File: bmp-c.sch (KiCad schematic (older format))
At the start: 61 parts, among them J1 USB_C_Receptacle_USB2.0, J2 Conn_01x10, J3 Conn_01x04, J4 JTAG-10, Q1 DMG1023DV, Q2 DMG1024UV, SW1 SW_SPST, U1 USBLC6-2P6, U2 SN74LVC2T45YZPR, U3 SN74LVC2T45YZPR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

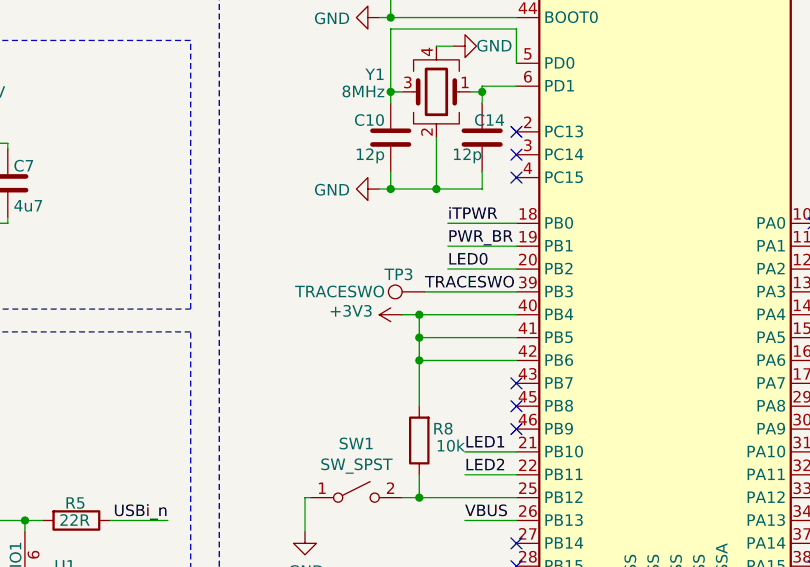
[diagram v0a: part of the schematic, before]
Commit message: remove SWO testpoint
Signed-off-by: Dominik Sliwa <dominik@e-plum.pl>
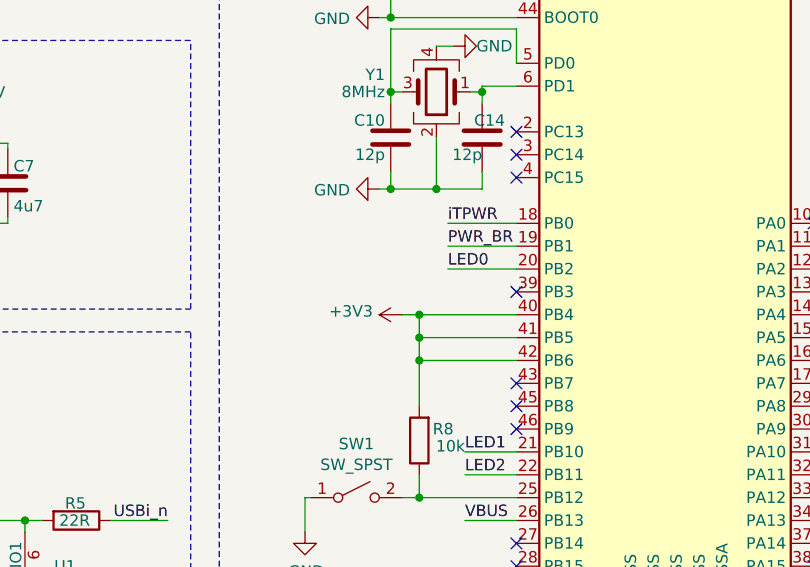
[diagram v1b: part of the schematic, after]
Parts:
- removed TP3: TRACESWO, TestPoint:TestPoint_Pad_D1.0mm, symbol Connector:TestPoint
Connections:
- net TRACESWO: no longer names the net of U6.39 (PB3)
- no-connect marks 13 -> 14
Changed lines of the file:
@@
 Wire Wire Line
 	5450 4375 5150 4375
-Wire Wire Line
-	5450 4475 5050 4475
 Text Label 5150 4275 0    50   ~ 0
 PWR_BR
 Text Label 5150 4375 0    50   ~ 0
 LED0
-Text Label 5050 4475 0    50   ~ 0
-TRACESWO
 Connection ~ 5025 4575
 Wire Wire Line
@@
 Text Label 9350 4825 0    50   ~ 0
 RST
-$Comp
-L Connector:TestPoint TP3
-U 1 1 5E7C2863
-P 5050 4475
-F 0 "TP3" V 5125 4525 50  0000 L CNN
-F 1 "TRACESWO" V 5050 4650 50  0000 L CNN
-F 2 "TestPoint:TestPoint_Pad_D1.0mm" H 5250 4475 50  0001 C CNN
-F 3 "~" H 5250 4475 50  0001 C CNN
-	1    5050 4475
-	0    -1   -1   0
-$EndComp
 Wire Wire Line
 	9575 3150 9350 3150
@@
 Text Label 5825 6225 2    50   ~ 0
 xTPWR
+NoConn ~ 5450 4475
 $EndSCHEMATC

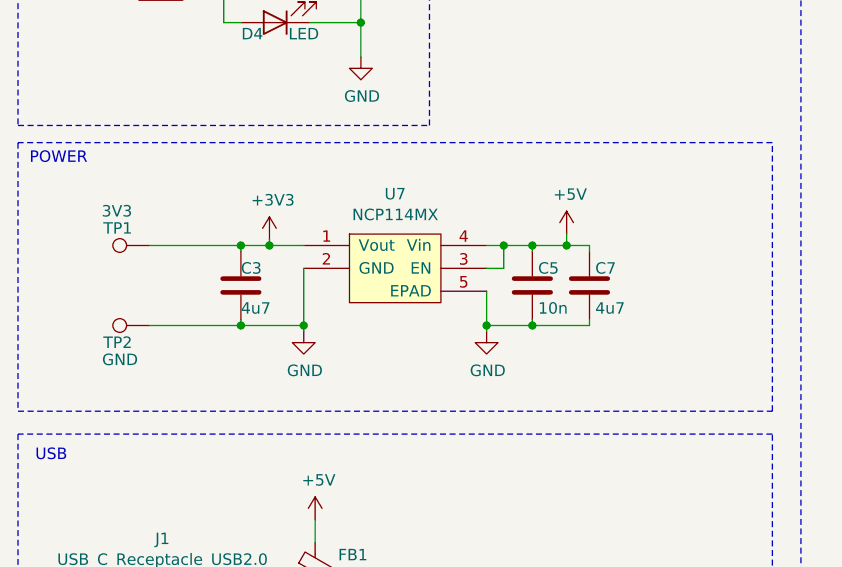
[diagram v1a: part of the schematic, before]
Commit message: use kicad library symbol for ncp114
Signed-off-by: Dominik Sliwa <dominik@e-plum.pl>
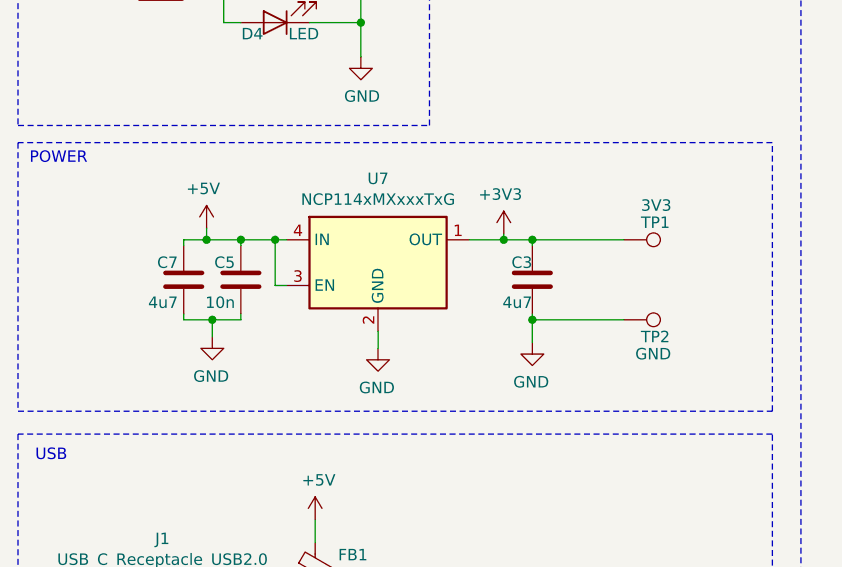
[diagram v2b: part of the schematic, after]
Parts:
- removed U7: NCP114MX, Package_DFN_QFN:UDFN-4_1x1mm_P0.65mm, symbol custom:NCP114MX
- added U7: NCP114xMXxxxTxG, Package_DFN_QFN:UDFN-4_1x1mm_P0.65mm, symbol Regulator_Linear:NCP114xMXxxxTxG
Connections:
- net +3V3: now also U7.1 (OUT)
- net +5V: now also U7.3 (EN), U7.4 (IN)
- net GND: now also U7.2 (GND), U7.5 (GND)
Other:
- moved on the sheet: C3, C5, C7, TP1, TP2
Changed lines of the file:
@@
 L Device:C C5
 U 1 1 5D514B13
-P 2975 4000
-F 0 "C5" H 3000 4075 50  0000 L CNN
-F 1 "10n" H 3000 3900 50  0000 L CNN
-F 2 "Capacitor_SMD:C_0402_1005Metric" H 3013 3850 50  0001 C CNN
-F 3 "~" H 2975 4000 50  0001 C CNN
-	1    2975 4000
-	1    0    0    -1
+P 1700 3975
+F 0 "C5" H 1725 4050 50  0000 L CNN
+F 1 "10n" H 1725 3875 50  0000 L CNN
+F 2 "Capacitor_SMD:C_0402_1005Metric" H 1738 3825 50  0001 C CNN
+F 3 "~" H 1700 3975 50  0001 C CNN
+	1    1700 3975
+	-1   0    0    -1
 $EndComp
 $Comp
 L Device:C C7
 U 1 1 5D515321
-P 3225 4000
-F 0 "C7" H 3250 4075 50  0000 L CNN
-F 1 "4u7" H 3250 3900 50  0000 L CNN
-F 2 "Capacitor_SMD:C_0603_1608Metric" H 3263 3850 50  0001 C CNN
-F 3 "~" H 3225 4000 50  0001 C CNN
-	1    3225 4000
-	1    0    0    -1
+P 1450 3975
+F 0 "C7" H 1475 4050 50  0000 L CNN
+F 1 "4u7" H 1475 3875 50  0000 L CNN
+F 2 "Capacitor_SMD:C_0603_1608Metric" H 1488 3825 50  0001 C CNN
+F 3 "~" H 1450 3975 50  0001 C CNN
+	1    1450 3975
+	-1   0    0    -1
 $EndComp
 $Comp
 L Device:C C3
 U 1 1 5D515C34
-P 1700 4000
-F 0 "C3" H 1700 4075 50  0000 L CNN
-F 1 "4u7" H 1700 3900 50  0000 L CNN
-F 2 "Capacitor_SMD:C_0603_1608Metric" H 1738 3850 50  0001 C CNN
-F 3 "~" H 1700 4000 50  0001 C CNN
-	1    1700 4000
-	1    0    0    -1
-$EndComp
-$Comp
-L custom:NCP114MX U7
-U 1 1 5D51FB0C
-P 2375 3875
-F 0 "U7" H 2375 4150 50  0000 C CNN
-F 1 "NCP114MX" H 2375 4059 50  0000 C CNN
-F 2 "Package_DFN_QFN:UDFN-4_1x1mm_P0.65mm" H 2375 3875 50  0001 C CNN
-F 3 "" H 2375 3875 50  0001 C CNN
-	1    2375 3875
-	1    0    0    -1
+P 2975 3975
+F 0 "C3" H 2975 4050 50  0000 L CNN
+F 1 "4u7" H 2975 3875 50  0000 L CNN
+F 2 "Capacitor_SMD:C_0603_1608Metric" H 3013 3825 50  0001 C CNN
+F 3 "~" H 2975 3975 50  0001 C CNN
+	1    2975 3975
+	-1   0    0    -1
 $EndComp
 $Comp
@@
 L power:GND #PWR09
 U 1 1 5D562287
-P 1975 4200
-F 0 "#PWR09" H 1975 3950 50  0001 C CNN
-F 1 "GND" H 1980 4027 50  0000 C CNN
-F 2 "" H 1975 4200 50  0001 C CNN
-F 3 "" H 1975 4200 50  0001 C CNN
-	1    1975 4200
-	1    0    0    -1
+P 2975 4250
+F 0 "#PWR09" H 2975 4000 50  0001 C CNN
+F 1 "GND" H 2980 4077 50  0000 C CNN
+F 2 "" H 2975 4250 50  0001 C CNN
+F 3 "" H 2975 4250 50  0001 C CNN
+	1    2975 4250
+	-1   0    0    -1
 $EndComp
 $Comp
 L power:GND #PWR016
 U 1 1 5D563C7B
-P 2775 4200
-F 0 "#PWR016" H 2775 3950 50  0001 C CNN
-F 1 "GND" H 2780 4027 50  0000 C CNN
-F 2 "" H 2775 4200 50  0001 C CNN
-F 3 "" H 2775 4200 50  0001 C CNN
-	1    2775 4200
-	1    0    0    -1
-$EndComp
-Wire Wire Line
-	1975 3825 1825 3825
-Wire Wire Line
-	1700 3825 1700 3850
-Wire Wire Line
-	1700 4150 1700 4175
-Wire Wire Line
-	1700 4175 1975 4175
-Wire Wire Line
-	1975 4175 1975 3925
-Wire Wire Line
-	1975 4175 1975 4200
-Connection ~ 1975 4175
-Wire Wire Line
-	2775 3925 2850 3925
-Wire Wire Line
-	2850 3925 2850 3825
-Wire Wire Line
-	2850 3825 2775 3825
-Wire Wire Line
-	2850 3825 2975 3825
-Wire Wire Line
-	3225 3825 3225 3850
-Connection ~ 2850 3825
-Wire Wire Line
-	2975 3850 2975 3825
-Connection ~ 2975 3825
-Wire Wire Line
-	2975 3825 3125 3825
-Wire Wire Line
-	2775 4025 2775 4175
-Wire Wire Line
-	2775 4175 2975 4175
-Wire Wire Line
-	2975 4175 2975 4150
-Connection ~ 2775 4175
-Wire Wire Line
-	2775 4175 2775 4200
-Wire Wire Line
-	3225 4150 3225 4175
-Wire Wire Line
-	3225 4175 2975 4175
-Connection ~ 2975 4175
+P 1575 4225
+F 0 "#PWR016" H 1575 3975 50  0001 C CNN
+F 1 "GND" H 1580 4052 50  0000 C CNN
+F 2 "" H 1575 4225 50  0001 C CNN
+F 3 "" H 1575 4225 50  0001 C CNN
+	1    1575 4225
+	-1   0    0    -1
+$EndComp
+Wire Wire Line
+	2700 3800 2850 3800
+Wire Wire Line
+	2975 3800 2975 3825
+Wire Wire Line
+	2975 4125 2975 4150
+Wire Wire Line
+	1450 3800 1450 3825
+Wire Wire Line
+	1700 3825 1700 3800
+Connection ~ 1700 3800
+Wire Wire Line
+	1700 3800 1550 3800
+Wire Wire Line
+	1700 4150 1700 4125
+Wire Wire Line
+	1450 4125 1450 4150
+Wire Wire Line
+	1450 4150 1575 4150
 $Comp
 L power:+5V #PWR019
 U 1 1 5D57BEAB
-P 3125 3775
-F 0 "#PWR019" H 3125 3625 50  0001 C CNN
-F 1 "+5V" H 3140 3948 50  0000 C CNN
-F 2 "" H 3125 3775 50  0001 C CNN
-F 3 "" H 3125 3775 50  0001 C CNN
-	1    3125 3775
-	1    0    0    -1
-$EndComp
-Wire Wire Line
-	3125 3775 3125 3825
-Connection ~ 3125 3825
-Wire Wire Line
-	3125 3825 3225 3825
+P 1550 3750
+F 0 "#PWR019" H 1550 3600 50  0001 C CNN
+F 1 "+5V" H 1565 3923 50  0000 C CNN
+F 2 "" H 1550 3750 50  0001 C CNN
+F 3 "" H 1550 3750 50  0001 C CNN
+	1    1550 3750
+	-1   0    0    -1
+$EndComp
+Wire Wire Line
+	1550 3750 1550 3800
+Connection ~ 1550 3800
+Wire Wire Line
+	1550 3800 1450 3800
 $Comp
 L power:+3V3 #PWR06
 U 1 1 5D57F918
-P 1825 3800
-F 0 "#PWR06" H 1825 3650 50  0001 C CNN
-F 1 "+3V3" H 1840 3973 50  0000 C CNN
-F 2 "" H 1825 3800 50  0001 C CNN
-F 3 "" H 1825 3800 50  0001 C CNN
-	1    1825 3800
-	1    0    0    -1
-$EndComp
-Wire Wire Line
-	1825 3800 1825 3825
-Connection ~ 1825 3825
-Wire Wire Line
-	1825 3825 1700 3825
+P 2850 3775
+F 0 "#PWR06" H 2850 3625 50  0001 C CNN
+F 1 "+3V3" H 2865 3948 50  0000 C CNN
+F 2 "" H 2850 3775 50  0001 C CNN
+F 3 "" H 2850 3775 50  0001 C CNN
+	1    2850 3775
+	-1   0    0    -1
+$EndComp
+Wire Wire Line
+	2850 3775 2850 3800
+Connection ~ 2850 3800
+Wire Wire Line
+	2850 3800 2975 3800
 Wire Notes Line
 	725  4550 4025 4550
@@
 	1    0    0    -1
 $EndComp
-Connection ~ 1700 3825
-Connection ~ 1700 4175
+Connection ~ 2975 3800
 Wire Wire Line
 	6100 2600 6100 2775
@@
 L Connector:TestPoint TP1
 U 1 1 5D7E637F
-P 1300 3825
-F 0 "TP1" V 1375 3900 50  0000 L CNN
-F 1 "3V3" V 1450 3900 50  0000 L CNN
-F 2 "TestPoint:TestPoint_Pad_D1.0mm" H 1500 3825 50  0001 C CNN
-F 3 "~" H 1500 3825 50  0001 C CNN
-	1    1300 3825
-	0    -1   -1   0
+P 3375 3800
+F 0 "TP1" V 3450 3875 50  0000 L CNN
+F 1 "3V3" V 3525 3875 50  0000 L CNN
+F 2 "TestPoint:TestPoint_Pad_D1.0mm" H 3575 3800 50  0001 C CNN
+F 3 "~" H 3575 3800 50  0001 C CNN
+	1    3375 3800
+	0    1    -1   0
 $EndComp
 $Comp
 L Connector:TestPoint TP2
 U 1 1 5D7E82A3
-P 1300 4175
-F 0 "TP2" V 1225 4250 50  0000 L CNN
-F 1 "GND" V 1150 4225 50  0000 L CNN
-F 2 "TestPoint:TestPoint_Pad_D1.0mm" H 1500 4175 50  0001 C CNN
-F 3 "~" H 1500 4175 50  0001 C CNN
-	1    1300 4175
-	0    -1   -1   0
+P 3375 4150
+F 0 "TP2" V 3300 4225 50  0000 L CNN
+F 1 "GND" V 3225 4200 50  0000 L CNN
+F 2 "TestPoint:TestPoint_Pad_D1.0mm" H 3575 4150 50  0001 C CNN
+F 3 "~" H 3575 4150 50  0001 C CNN
+	1    3375 4150
+	0    1    -1   0
 $EndComp
 NoConn ~ 5450 3775
@@
 	5025 4775 5450 4775
 Wire Wire Line
-	1300 4175 1700 4175
-Wire Wire Line
-	1300 3825 1700 3825
+	3375 4150 2975 4150
+Wire Wire Line
+	3375 3800 2975 3800
 Text Label 5825 6225 2    50   ~ 0
 xTPWR
 NoConn ~ 5450 4475
+$Comp
+L Regulator_Linear:NCP114xMXxxxTxG U7
+U 1 1 5D71C52E
+P 2300 3900
+F 0 "U7" H 2300 4267 50  0000 C CNN
+F 1 "NCP114xMXxxxTxG" H 2300 4176 50  0000 C CNN
+F 2 "Package_DFN_QFN:UDFN-4_1x1mm_P0.65mm" H 3100 3500 50  0001 C CNN
+F 3 "https://www.onsemi.com/pub/Collateral/NCP114-D.PDF" H 2300 3900 50  0001 C CNN
+	1    2300 3900
+	1    0    0    -1
+$EndComp
+$Comp
+L power:GND #PWR048
+U 1 1 5D7FABA9
+P 2300 4275
+F 0 "#PWR048" H 2300 4025 50  0001 C CNN
+F 1 "GND" H 2305 4102 50  0000 C CNN
+F 2 "" H 2300 4275 50  0001 C CNN
+F 3 "" H 2300 4275 50  0001 C CNN
+	1    2300 4275
+	-1   0    0    -1
+$EndComp
+Wire Wire Line
+	1700 3800 1850 3800
+Wire Wire Line
+	2975 4250 2975 4150
+Connection ~ 2975 4150
+Wire Wire Line
+	2300 4275 2300 4200
+Wire Wire Line
+	1575 4225 1575 4150
+Connection ~ 1575 4150
+Wire Wire Line
+	1575 4150 1700 4150
+Wire Wire Line
+	1900 4000 1850 4000
+Wire Wire Line
+	1850 4000 1850 3800
+Connection ~ 1850 3800
+Wire Wire Line
+	1850 3800 1900 3800
 $EndSCHEMATC
